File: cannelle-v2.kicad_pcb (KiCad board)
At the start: 2 copper layers, 60 parts, among them P1 USB_OTG, P2 CONN_02X04, P3 CONN_02X22, P4 CONN_02X22, SW1 SW_PUSH, U2 ATMEGA16U4-A, U3 SST25VF020B, U4 LD1117S12TR, U5 NCP1117ST33T3G, U6 ICE40HX1K-VQ100, X1 8MHz, X2 IQXO/7X

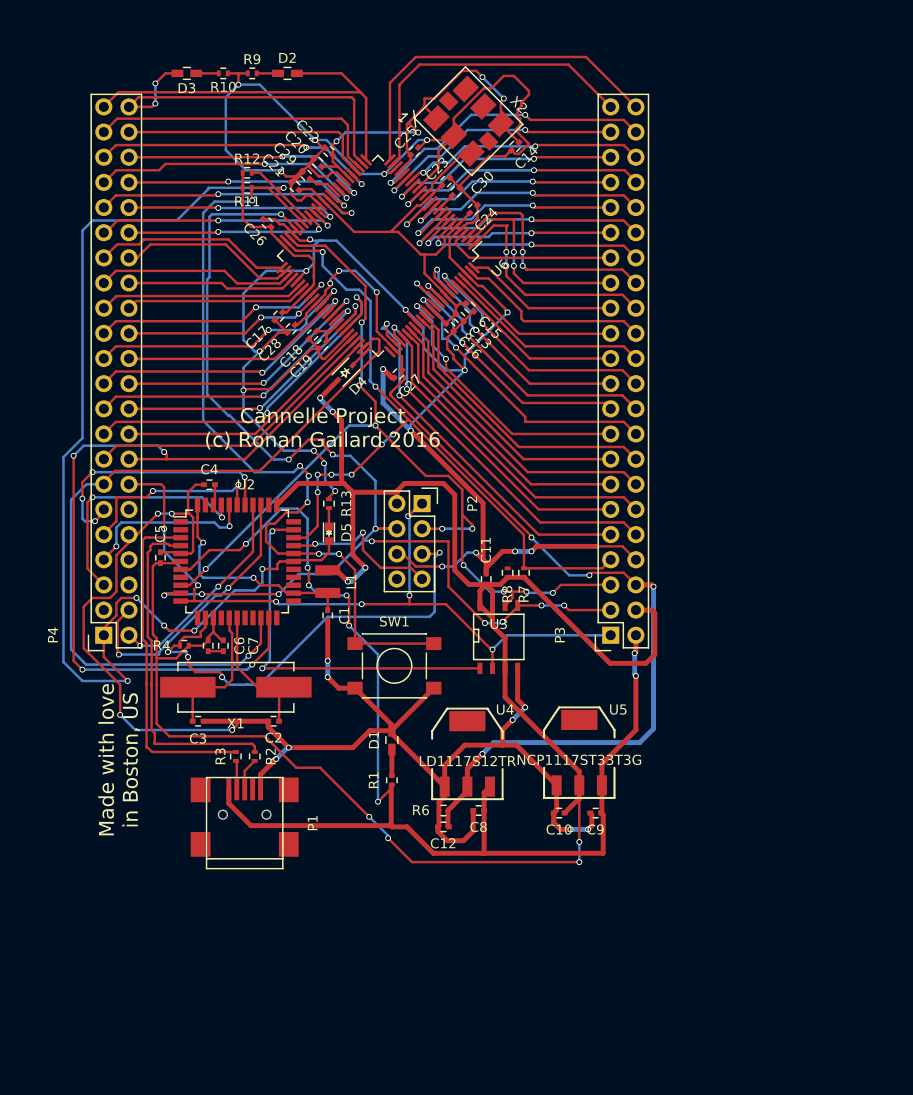
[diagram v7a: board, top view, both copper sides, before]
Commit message: Connect all pads and edge cuts
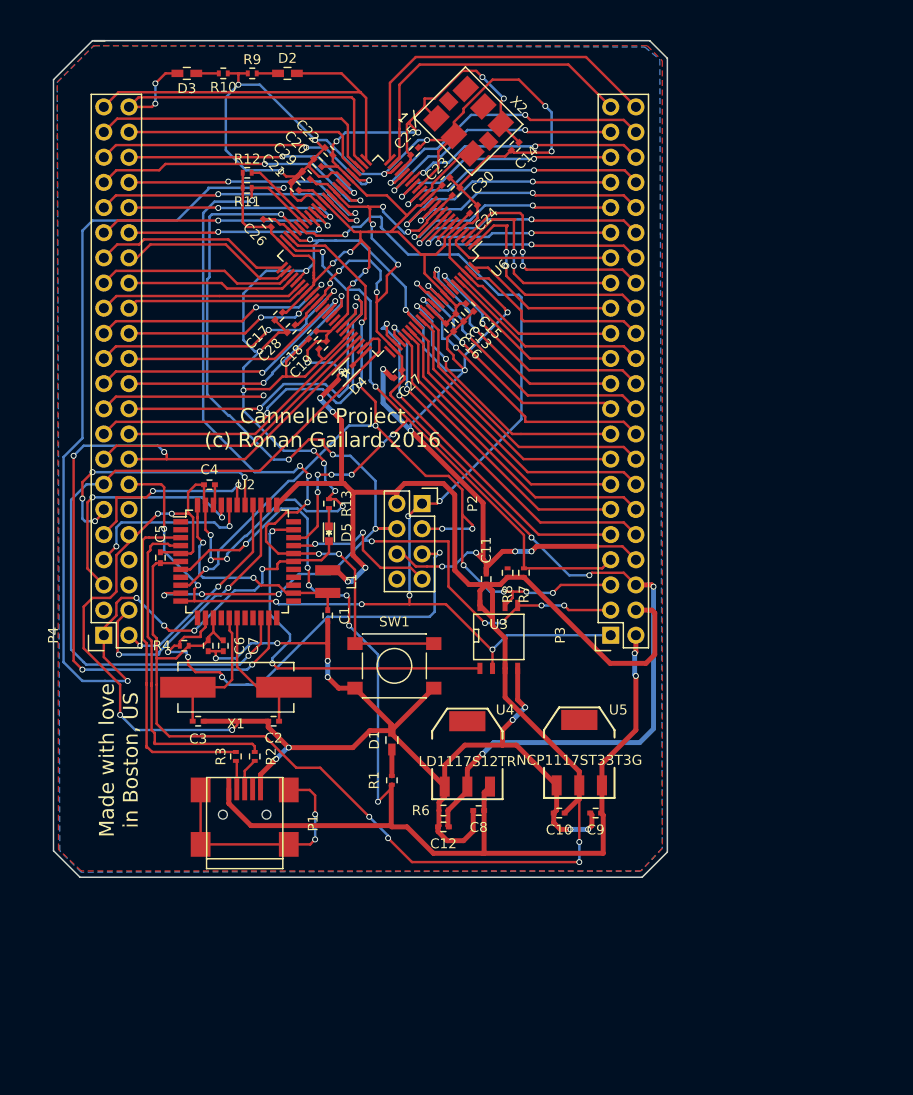
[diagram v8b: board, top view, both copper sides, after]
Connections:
- P2 pad 5: /RST_AVR -> Net-(P2-Pad5)
- P4 pad 3: /FPGA/ICE40_RESET -> /FPGA/P4_03
- U6 pad 66: /FPGA/P4_19 -> Net-(U6-Pad66)
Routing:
- net /FPGA/ICE40_SDO: track 71.9 -> 121.3 mm, vias 7 -> 9
- net GND: track 445.6 -> 491.4 mm, vias 33 -> 41
- net Net-(P2-Pad5): track 0.00 -> 38.4 mm, vias 0 -> 3
- net /RST_AVR: track 46.6 -> 8.22 mm, vias 4 -> 1
- net +3V3: track 310.0 -> 345.0 mm, vias 12 -> 18
- net +1V2: track 105.7 -> 134.1 mm, vias 7 -> 11
- net Net-(P1-Pad6): track 0.00 -> 24.6 mm, vias 0 -> 2
- net /FPGA/P4_19: track 30.4 -> 16.7 mm, vias 2 -> 1
- net /FPGA/P4_17: track 37.7 -> 42.9 mm
- net /FPGA/P4_20: track 30.5 -> 35.6 mm
- net /FPGA/P4_14: track 3.68 -> 7.87 mm
- net /FPGA/P4_38: track 24.5 -> 28.0 mm
- net /FPGA/P4_37: track 28.1 -> 31.0 mm
- net /FPGA/P4_35: track 29.5 -> 31.5 mm
- net /FPGA/P4_39: track 29.6 -> 31.2 mm
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- added copper zone on B.Cu, net GND
- added copper zone on F.Cu, net GND
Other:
- board outline added: 62 x 84.5 mm
